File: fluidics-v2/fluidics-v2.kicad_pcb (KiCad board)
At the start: 4 copper layers, 127 x 127.2 mm, 177 parts, among them IC1 MCZ33996EKR2, IC2 ADUM1250WSRZ-RL7, IC3 HSCDRRN001BDSA3, IC4 HSCDRRN001BDSA3, IC5 HSCDRRN001BDSA3, IC6 HSCDRRN001BDSA3, J1 PJ-063AH, J10 87832-1010, J11 0705430001, J12 87832-1010, J13 0705430001, J14 87832-1010, J15 0533980671, J16 0705430001, J17 0533980671, J18 87832-1010, J19 0705430001, J2 B6B-ZR-SM4-TF, J20 0533980671, J21 87832-1010, J22 0705430001, J23 0533980671, J3 A-DS_15_A_KG-T4S, J4 B6B-ZR-SM4-TF, J5 1860280, J6 Conn_02x14_Counter_Clockwise, J7 Conn_02x03_Odd_Even, J8 705430039, J9 522712079, SW1 D6C90F1LFS, U10 LTC4311CSC6-TRPBF, U11 MAX3221, U12 CD4050BDR, U13 TC7PZ17FU, U16 LTC4316CMS-TRPBF, U2 Teensy4.1, U3 AP7366EA-33W5-7, U4 D24V10FX, U6 LTC4311CSC6-TRPBF, U7 TCA9539PWR, U8 LTC4311CSC6-TRPBF, U9 LTC4311CSC6-TRPBF

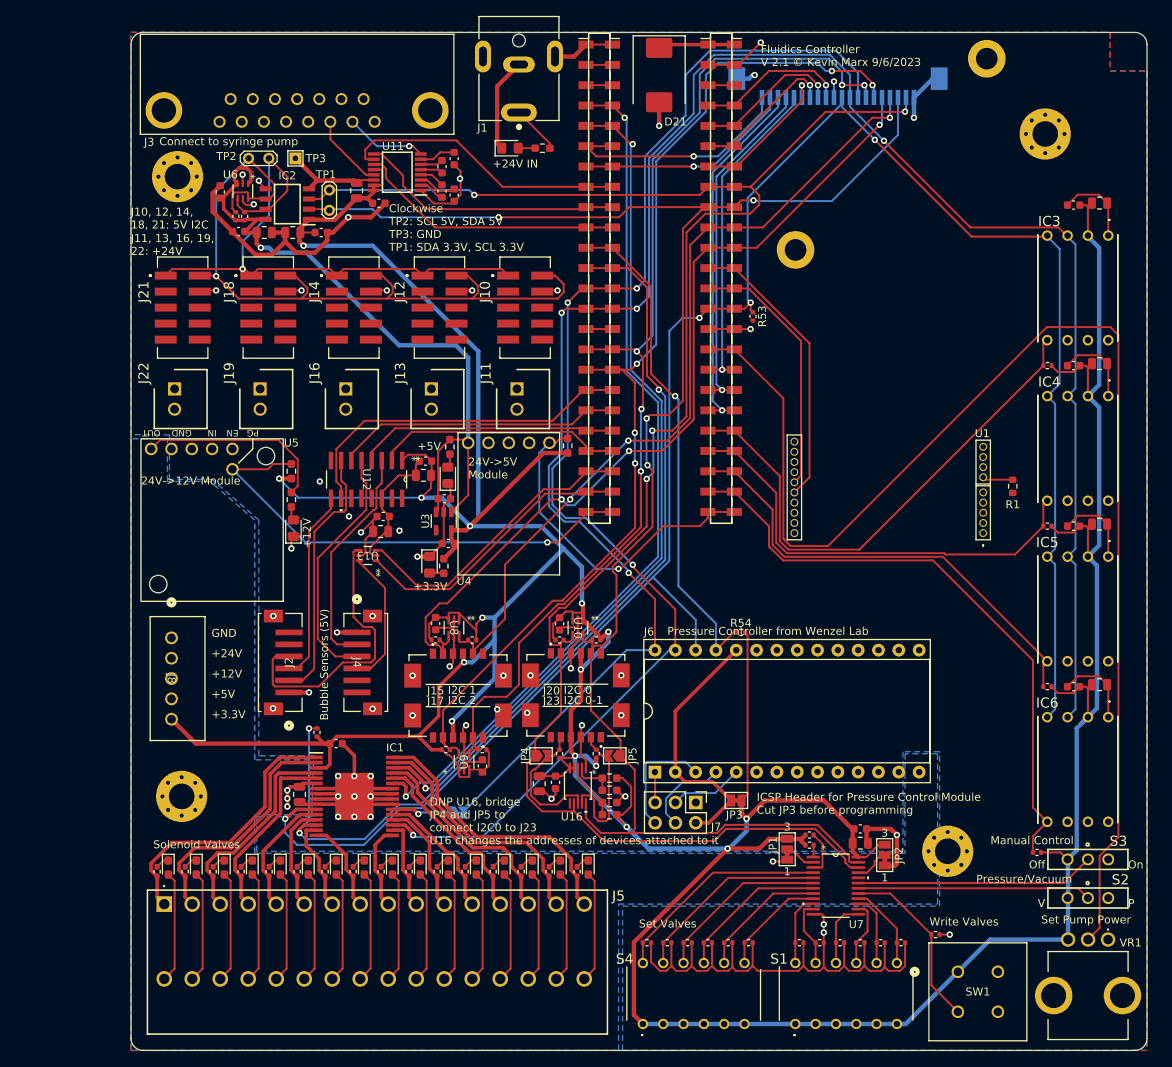
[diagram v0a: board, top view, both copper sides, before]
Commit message: V3: strip to minimal fluidics config, add 6th selector valve, fix lib paths
Reduce the V2 fluidics controller to a minimal build and extend the
selector-valve bank:

- Remove disc-pump driver (U1, M1); keep the syringe pump only
- Remove the solenoid-valve subsystem (MCZ33996 IC1 + D5-D20 + R6-R21
  + connector J5) -- 16 solenoids -> 0
- Remove all SPI pressure sensors (IC3-IC6 and their passives) -- 4 -> 0
- Reduce I2C flow sensors 4 -> 3 (drop connector J17)
- Add a 6th IDEX selector-valve channel (connectors J24/J25) on the
  shared isolated-I2C + 24V bus
- Remove the Wenzel-lab pressure-controller daughter board interface
  (J6, J7/ICSP, J8, JP3)
- Remove the manual-control block (switches S1-S4, push-button SW1,
  potentiometer VR1, TCA9539 U7, pull-ups, jumpers)
- Remove the 24V->12V converter (U5 + indicator D1/R2 + power-good R52);
  no remaining 12V load after the above

Net component count: 177 -> 86 footprints. DRC: 0 unconnected.

Tooling/portability fixes:
- Rewrite fp-lib-table and sym-lib-table: replace the original author's
  hardcoded absolute paths (/home/octopi-codex/...) with ${KIPRJMOD}-
  relative URIs so the libraries resolve on any machine
- Migrate the project to KiCad 10 format
- Add .gitignore for KiCad lock/autosave/cache and editor history files
- Add fluidics-v3-schematic.pdf (rendered schematic for review)

Co-Authored-By: Claude Opus 4.8 (1M context) <noreply@anthropic.com>
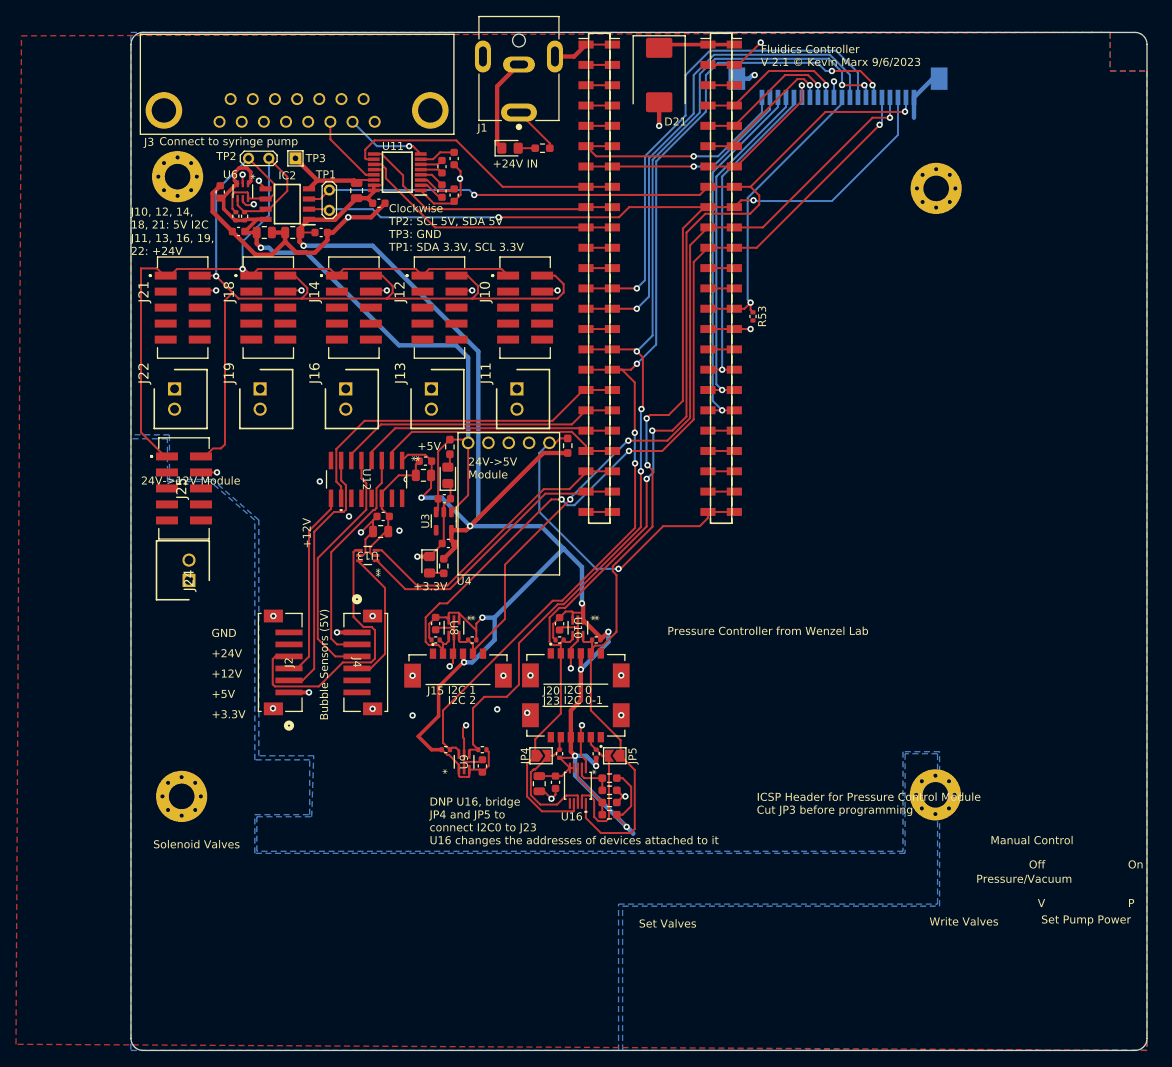
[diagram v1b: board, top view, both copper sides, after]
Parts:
- removed C10, C3, C31, C32, C33, C34: 0.1u, Capacitor_SMD:C_0603_1608Metric
- removed C11, C36, C37, C38, C39, C4: 1u, Capacitor_SMD:C_0805_2012Metric
- removed D1: LED, LED_SMD:LED_0805_2012Metric_Pad1.15x1.40mm_HandSolder
- removed D10, D11, D12, D13, D14, D15, D16, D17, D18, D19, D20, D5, D6, D7, D8, D9: LED, LED_SMD:LED_0603_1608Metric_Pad1.05x0.95mm_HandSolder
- removed IC1: MCZ33996EKR2, NXP:SOP65P1030X265-33N
- removed IC3, IC4, IC5, IC6: HSCDRRN001BDSA3, HSCDRRN001BDSA3:HSCDRRN001BDSA3
- removed J17: 0533980671, molex_connectors:MOLEX_0533980671
- removed J5: 1860280, phoenix_2:1860280
- removed J6: Conn_02x14_Counter_Clockwise, Package_DIP:DIP-28_W15.24mm_Socket
- removed J7: Conn_02x03_Odd_Even, Connector_PinHeader_2.54mm:PinHeader_2x03_P2.54mm_Vertical
- removed J8: 705430039, 0705430004:70543-0039_MOL
- removed JP1, JP2: SolderJumper_3_Bridged12, Jumper:SolderJumper-3_P1.3mm_Bridged12_Pad1.0x1.5mm_NumberLabels
- removed JP3: SolderJumper_2_Bridged, Jumper:SolderJumper-2_P1.3mm_Bridged_Pad1.0x1.5mm
- removed JP6: SolderJumper_2_Open, Jumper:SolderJumper-2_P1.3mm_Open_TrianglePad1.0x1.5mm
- removed M1: ~, TTP Ventus:Pump Mount
- removed R1: 0, Resistor_SMD:R_0603_1608Metric
- removed R10, R11, R12, R13, R14, R15, R16, R17, R18, R19, R20, R21, R6, R7, R8, R9: 3.3k, Resistor_SMD:R_0402_1005Metric_Pad0.72x0.64mm_HandSolder
- removed R2: 20k, Resistor_SMD:R_0603_1608Metric_Pad0.98x0.95mm_HandSolder
- removed R24, R25, R26, R27, R28, R29, R30, R31, R32, R33, R34, R35, R36, R37, R38: 10k, Resistor_SMD:R_0402_1005Metric
- removed R52: 47k, Resistor_SMD:R_0603_1608Metric_Pad0.98x0.95mm_HandSolder
- removed R54, R55, R56, R57, R58, R59: 4.7k, Resistor_SMD:R_0402_1005Metric
- removed S1, S4: 210-6MS, 210-6MS:2106MS
- removed S2, S3: 450301014042, wurth:450301014042
- removed SW1: D6C90F1LFS, pushbutton:SW4_D6C90F1LFS_CNK
- removed U1: ~, TTP Ventus:Disc_Pump_Driver_PCB
- removed U5: ~, D36V28Fx:D36V28Fx
- removed U7: TCA9539PWR, TCA9539PWR:PW24
- removed VR1: PTV09A-4020U-B103, bourns:PTV09A4015FB103
- added J24: 0705430001, molex_connectors:SHDR2W64P0X254_1X2_737X660X1181P, F.Cu at (22.0, 84.0)
- added J25: 87832-1010, molex_connectors:878321010, F.Cu at (21.4, 72.5)
- moved H1 15.2 mm to (115.4, 35.0)
- moved H3 7.22 mm to (115.3, 110.8)
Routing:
- net +3.3V: track 632.7 -> 266.4 mm, vias 15 -> 11
- net +12V: track 252.9 -> 0.00 mm, vias 3 -> 0
- net /SPI_SCK: track 249.7 -> 37.7 mm, vias 4 -> 1
- net /SPI_MISO: track 246.3 -> 63.0 mm, vias 4 -> 1
- net GND: track 363.1 -> 184.4 mm, vias 52 -> 37
- net /POT_ANALOG: track 160.7 -> 3.30 mm
- net /SPI_~{CS}_VALVES: track 121.4 -> 3.30 mm, vias 3 -> 0
- net /VALVES_~{RST}: track 109.1 -> 3.30 mm, vias 2 -> 0
- net /VALVES_PWM: track 107.4 -> 3.30 mm, vias 2 -> 0
- net /SPI_MOSI: track 163.5 -> 62.6 mm, vias 4 -> 1
- net /~{CS}3: track 76.3 -> 3.30 mm
- net /~{CS}0: track 65.7 -> 3.30 mm
- net /SPI_~{CS}_PRESS: track 62.6 -> 3.30 mm, vias 1 -> 0
- net /PG-12V: track 60.7 -> 3.30 mm, vias 1 -> 0
- net /~{CS}2: track 58.2 -> 3.30 mm
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- added copper zone on B.Cu, net (none)
- removed copper zone on B.Cu, net +12V

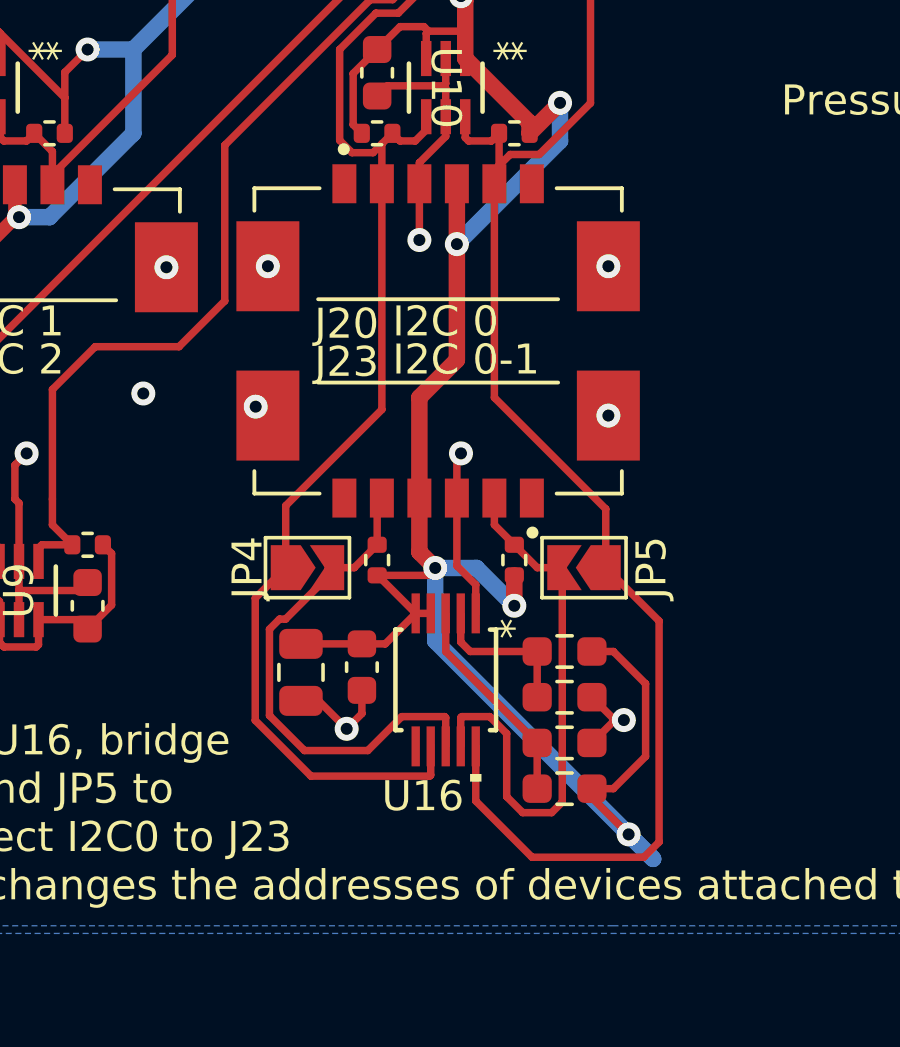
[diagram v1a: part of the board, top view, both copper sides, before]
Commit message: @ WIP: continue strip-down — empty sensors sheet, drop 11 PCB footprints
Recovered in-progress work from the previous KiCad session (restored via
KiCad session recovery). This is mid-edit, not a finished config:
- sensors.kicad_sch: 17 -> 0 symbols (sheet fully emptied)
- fluidics-v2.kicad_pcb: 86 -> 75 footprints
- fluidics-v2.kicad_sch: minor net/sheet cleanup

Schematic + libraries validated with kicad-cli sch export netlist (exit 0).

Co-Authored-By: Claude Opus 4.8 (1M context) <noreply@anthropic.com>
@
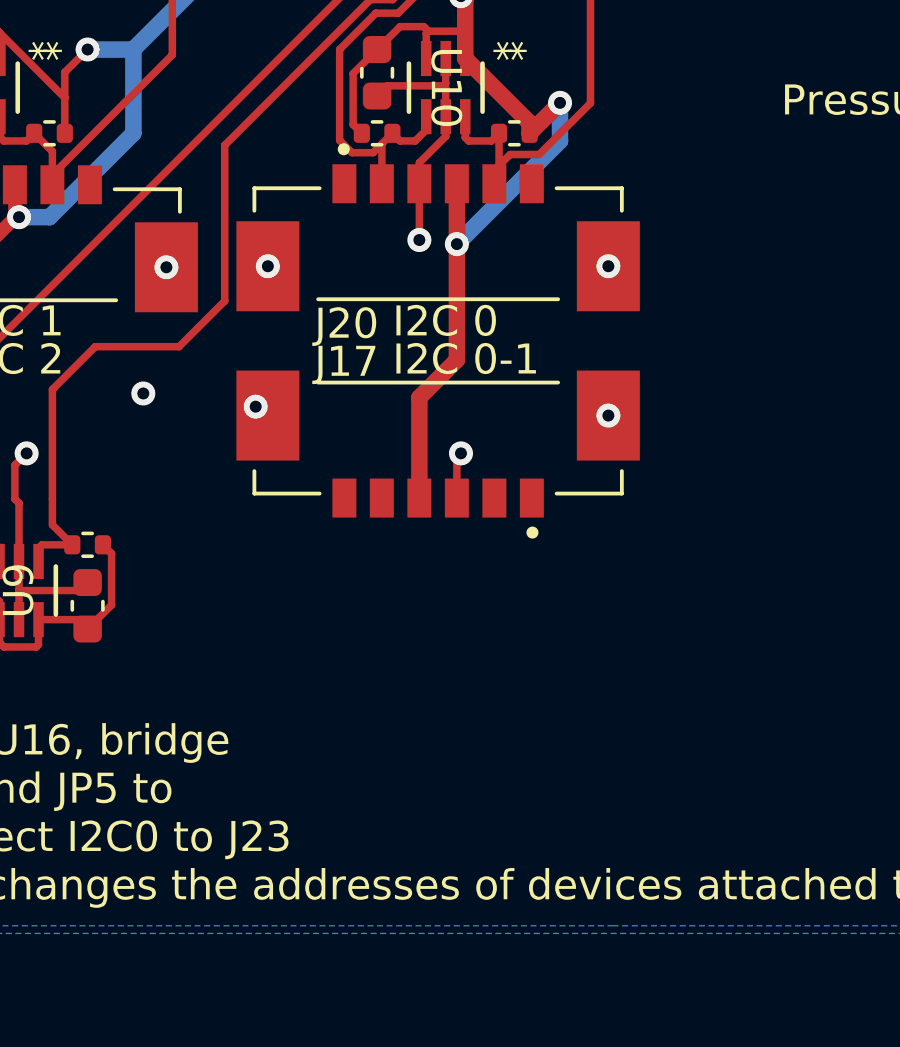
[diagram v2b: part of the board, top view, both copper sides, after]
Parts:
- removed C30: 0.1u, Capacitor_SMD:C_0603_1608Metric
- removed C35: 1u, Capacitor_SMD:C_0805_2012Metric
- removed JP4, JP5: SolderJumper_2_Open, Jumper:SolderJumper-2_P1.3mm_Open_TrianglePad1.0x1.5mm
- removed R45: 976k, Resistor_SMD:R_0603_1608Metric_Pad0.98x0.95mm_HandSolder
- removed R46: DNP, Resistor_SMD:R_0603_1608Metric_Pad0.98x0.95mm_HandSolder
- removed R47: 102k, Resistor_SMD:R_0603_1608Metric_Pad0.98x0.95mm_HandSolder
- removed R48: 0, Resistor_SMD:R_0603_1608Metric_Pad0.98x0.95mm_HandSolder
- removed R49, R50: 4.7k, Resistor_SMD:R_0402_1005Metric
- removed U16: LTC4316CMS-TRPBF, addresstranslator:MSOP-10_MS_LIT
- renumbered J23 to J17
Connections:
- J17 pad 2: /Sensors/SCL_OUT -> /SCL2
- J17 pad 5: /Sensors/SDA_OUT -> /SDA2
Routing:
- net +3.3V: track 266.4 -> 228.3 mm, vias 11 -> 8
- net /SCL: track 185.1 -> 152.0 mm
- net /SDA: track 187.4 -> 160.2 mm
- net /Sensors/SCL_OUT: track 18.6 -> 0.00 mm
- net /Sensors/SDA_OUT: track 17.2 -> 0.00 mm
- net GND: track 184.4 -> 174.5 mm, vias 37 -> 35
- net Net-(U16-XORL): track 7.10 -> 0.00 mm
- net Net-(U16-XORH): track 5.16 -> 0.00 mm

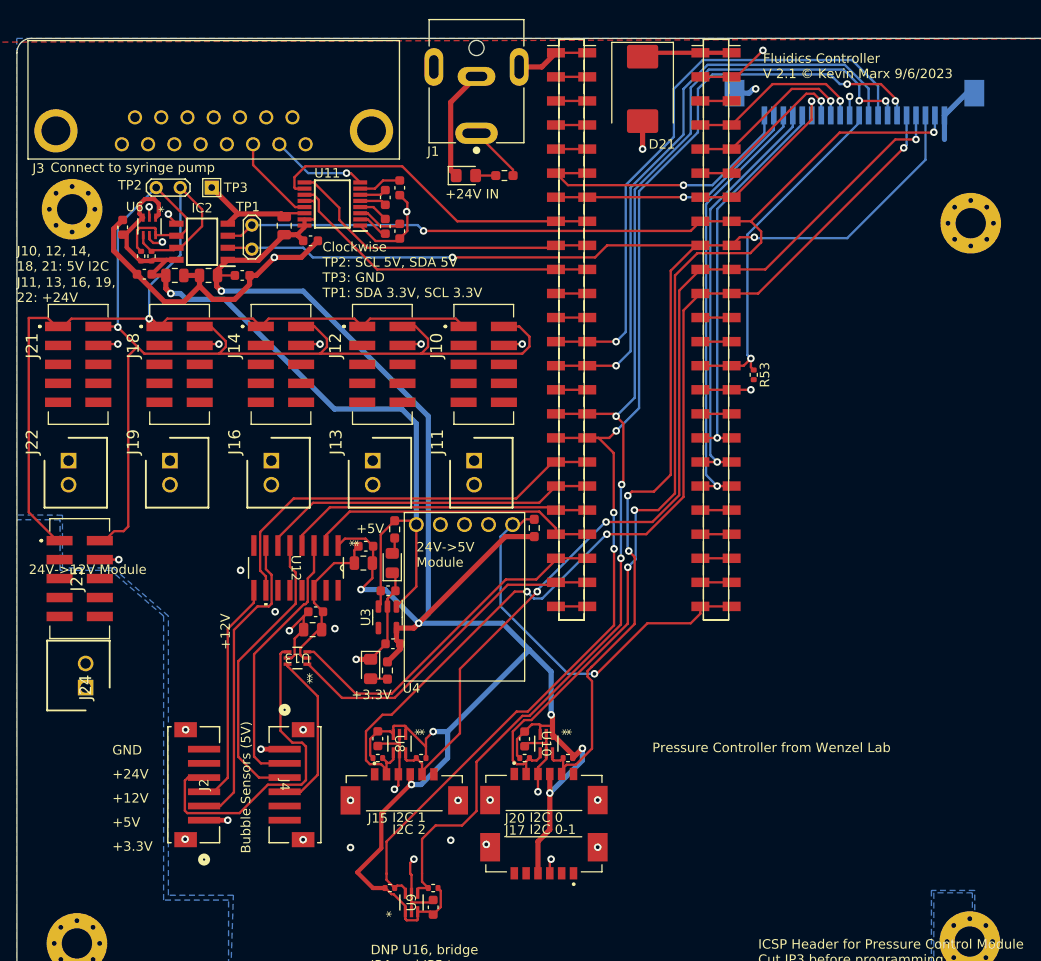
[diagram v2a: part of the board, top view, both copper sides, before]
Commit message: @ Remove J9 daughterboard connector; restore Back GND plane; fix thermals
- Delete J9 (20-pin FPC to motor-control daughterboard) from PCB + schematic;
  its SPI/GPIO went nowhere else on-board (75 -> 74 footprints)
- Remove orphaned GPIO_1-9 / SPI_MOSI / SPI_MISO copper (72 tracks, 11 vias)
  plus the ex-J9 dangling stub vias on the I2C/SCK buses
- Reassign the floating no-net Back pour to GND: clears isolated_copper and
  restores a continuous back-side ground plane
- Set U4/J15/D2 GND pads to solid zone connection: clears starved_thermal
- DRC: 229 -> 217 violations. starved_thermal 3->0, isolated_copper 1->0,
  via_dangling 7->0. Remaining ~217 are cosmetic silk/courtyard/library
  warnings inherited from upstream.

Co-Authored-By: Claude Opus 4.8 (1M context) <noreply@anthropic.com>
@
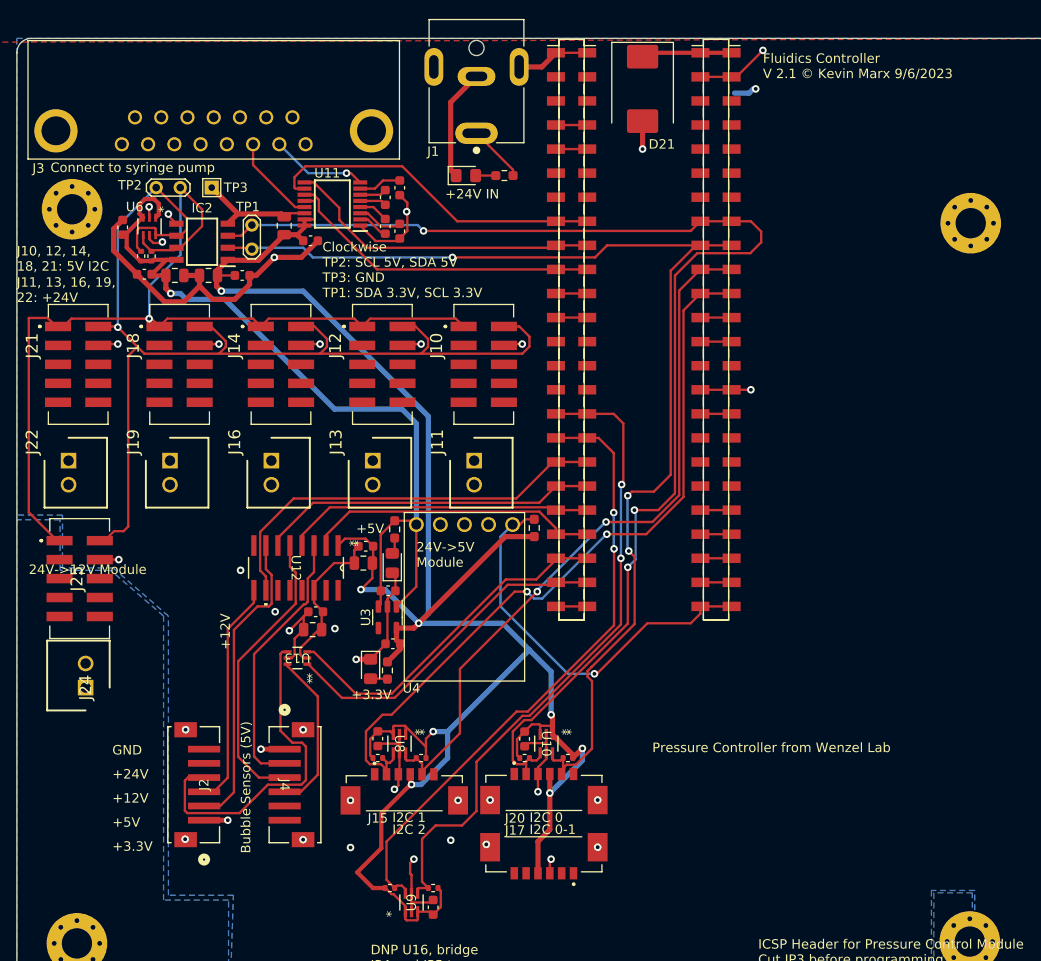
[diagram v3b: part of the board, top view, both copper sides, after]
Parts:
- removed J9: 522712079, 0522712079:CON_522712079_MOL
- removed R53: 4.7k, Resistor_SMD:R_0402_1005Metric
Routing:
- net /SDA2: track 132.9 -> 65.1 mm, vias 5 -> 2
- net /SCL2: track 132.5 -> 68.9 mm, vias 5 -> 2
- net /SPI_MISO: track 63.0 -> 0.00 mm, vias 1 -> 0
- net /SPI_MOSI: track 62.6 -> 0.00 mm, vias 1 -> 0
- net /GPIO_7: track 46.3 -> 0.00 mm, vias 1 -> 0
- net /GPIO_6: track 43.8 -> 0.00 mm, vias 1 -> 0
- net /GPIO_5: track 41.1 -> 0.00 mm, vias 1 -> 0
- net /SPI_SCK: track 37.7 -> 0.00 mm, vias 1 -> 0
- net /SCL: track 152.0 -> 121.5 mm, vias 4 -> 3
- net /GPIO_9: track 30.0 -> 0.00 mm, vias 1 -> 0
- net /SCL1: track 107.5 -> 78.9 mm, vias 3 -> 2
- net /SDA1: track 103.3 -> 75.3 mm, vias 3 -> 2
- net /GPIO_8: track 27.5 -> 0.00 mm, vias 1 -> 0
- net /SDA: track 160.2 -> 134.7 mm, vias 4 -> 3
- net /GPIO_1: track 19.0 -> 0.00 mm, vias 1 -> 0
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- removed copper zone on B.Cu, net (none)
